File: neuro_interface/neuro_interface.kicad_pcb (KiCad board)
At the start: 2 copper layers, 80 x 80 mm, 90 parts, among them J1 Connector B, J2 Connector A

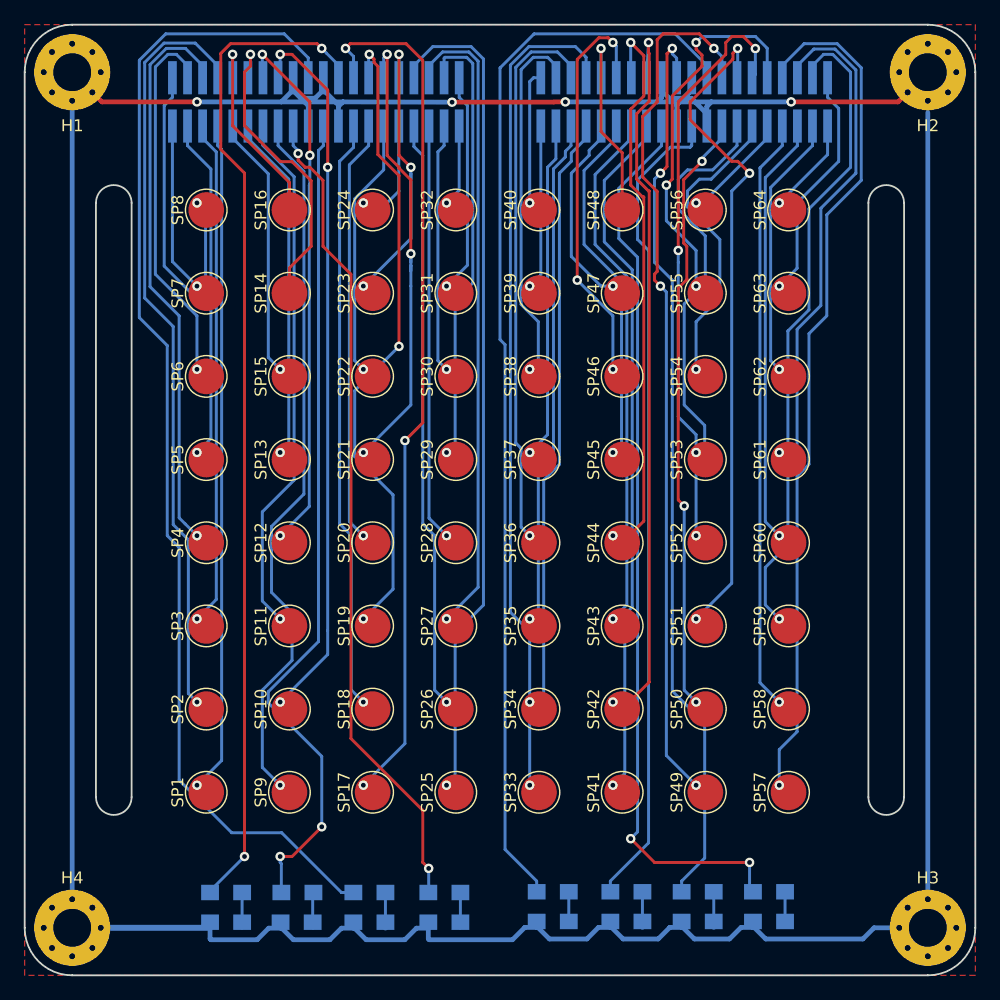
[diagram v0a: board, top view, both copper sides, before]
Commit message: added ground plane on non-skin side
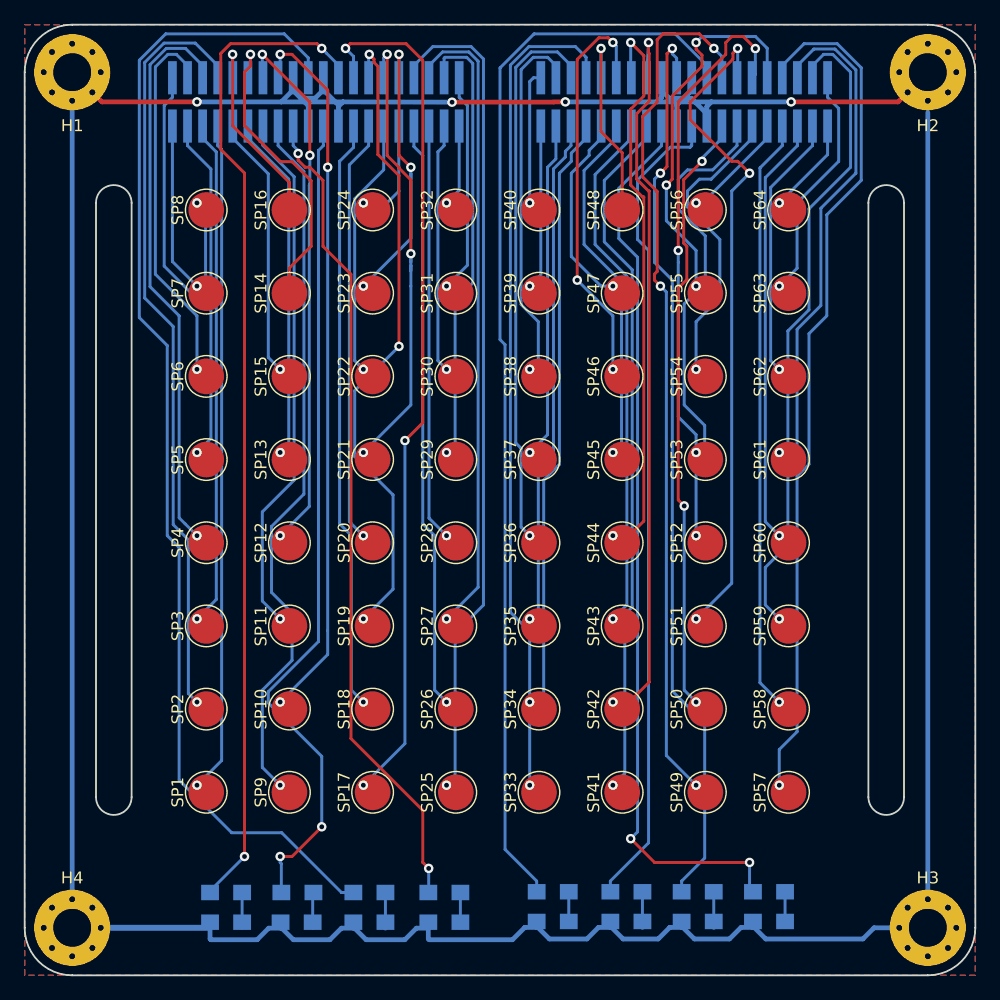
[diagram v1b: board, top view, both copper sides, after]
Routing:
- added copper zone on B.Cu, net GND
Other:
- board text added: "v.0.1 2020.01.26"
- board text removed: "v.0.1 2019.12.13"
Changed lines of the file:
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@@
   (general
     (thickness 1.6)
-    (drawings 23)
+    (drawings 24)
     (tracks 784)
     (zones 0)
@@
       (xy 11.487147 4.67424) (xy 11.737696 4.706276) (xy 12.022845 4.697354)) (layer B.SilkS) (width 0.01))
   )
-  (gr_text "v.0.1 2019.12.13" (at 109.18335 98.542335) (layer B.SilkS)
+  (dimension 3 (width 0.3) (layer Dwgs.User)
+    (gr_text "3.000 mm" (at 77.5 69.9) (layer Dwgs.User)
+      (effects (font (size 1.5 1.5) (thickness 0.3)))
+    )
+    (feature1 (pts (xy 76 75) (xy 76 71.413579)))
+    (feature2 (pts (xy 79 75) (xy 79 71.413579)))
+    (crossbar (pts (xy 79 72) (xy 76 72)))
+    (arrow1a (pts (xy 76 72) (xy 77.126504 71.413579)))
+    (arrow1b (pts (xy 76 72) (xy 77.126504 72.586421)))
+    (arrow2a (pts (xy 79 72) (xy 77.873496 71.413579)))
+    (arrow2b (pts (xy 79 72) (xy 77.873496 72.586421)))
+  )
+  (gr_text "v.0.1 2020.01.26" (at 109.18335 98.542335) (layer B.SilkS)
     (effects (font (size 1 1) (thickness 0.25)) (justify mirror))
   )
@@
     (polygon
       (pts
+        (xy 70 60) (xy 150 60) (xy 150 140) (xy 70 140)
+      )
+    )
+  )
+  (zone (net 2) (net_name GND) (layer B.Cu) (hatch edge 0.508)
+    (connect_pads (clearance 0.4))
+    (min_thickness 0.254)
+    (fill yes (arc_segments 16) (thermal_gap 0.508) (thermal_bridge_width 0.508))
+    (polygon
+      (pts
